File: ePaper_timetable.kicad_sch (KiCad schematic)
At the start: 70 parts, among them J1 USB_C_Receptacle_USB2.0, J2 Conn_01x01_Pin, J3 52435-2471, J4 Conn_01x03_Socket, J5 Charging input - 5V, J6 Conn_01x03_Socket, J7 Conn_01x03_Socket, J8 Conn_01x04_Socket, J9 Battery connector, Q1 BSS138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

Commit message: layout proposition
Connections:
- net Interconnect: now reaches Q3.1, Q3.8
- net USB_DM renamed USB-
- net USB_DP renamed USB+
- no-connect marks 20 -> 19
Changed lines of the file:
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@@
   (no_connect (at 35.56 86.36))
   (no_connect (at 76.2 66.04))
-  (no_connect (at 219.71 131.445))
   (no_connect (at 76.2 45.72))
   (no_connect (at 63.5 247.65))
@@
     (effects (font (size 1.27 1.27)) (justify right bottom))
   )
-  (label "USB_DP" (at 55.88 24.765 90) (fields_autoplaced)
+  (label "USB+" (at 55.88 24.765 90) (fields_autoplaced)
     (effects (font (size 1.27 1.27)) (justify left bottom))
   )
@@
     (effects (font (size 1.27 1.27)) (justify left bottom))
   )
-  (label "USB_DP" (at 104.14 237.49 0) (fields_autoplaced)
+  (label "USB+" (at 104.14 237.49 0) (fields_autoplaced)
     (effects (font (size 1.27 1.27)) (justify left bottom))
   )
@@
     (effects (font (size 1.27 1.27)) (justify left bottom))
   )
+  (label "Interconnect" (at 219.71 131.445 0) (fields_autoplaced)
+    (effects (font (size 1.27 1.27)) (justify left bottom))
+  )
   (label "BOOTSEL" (at 63.5 24.765 90) (fields_autoplaced)
     (effects (font (size 1.27 1.27)) (justify left bottom))
@@
     (effects (font (size 1.27 1.27)) (justify right bottom))
   )
-  (label "USB_DM" (at 104.14 232.41 0) (fields_autoplaced)
-    (effects (font (size 1.27 1.27)) (justify left bottom))
-  )
-  (label "USB_DM" (at 53.34 24.765 90) (fields_autoplaced)
-    (effects (font (size 1.27 1.27)) (justify left bottom))
-  )
+  (label "USB-" (at 104.14 232.41 0) (fields_autoplaced)
+    (effects (font (size 1.27 1.27)) (justify left bottom))
+  )
+  (label "USB-" (at 53.34 24.765 90) (fields_autoplaced)
+    (effects (font (size 1.27 1.27)) (justify left bottom))
+  )

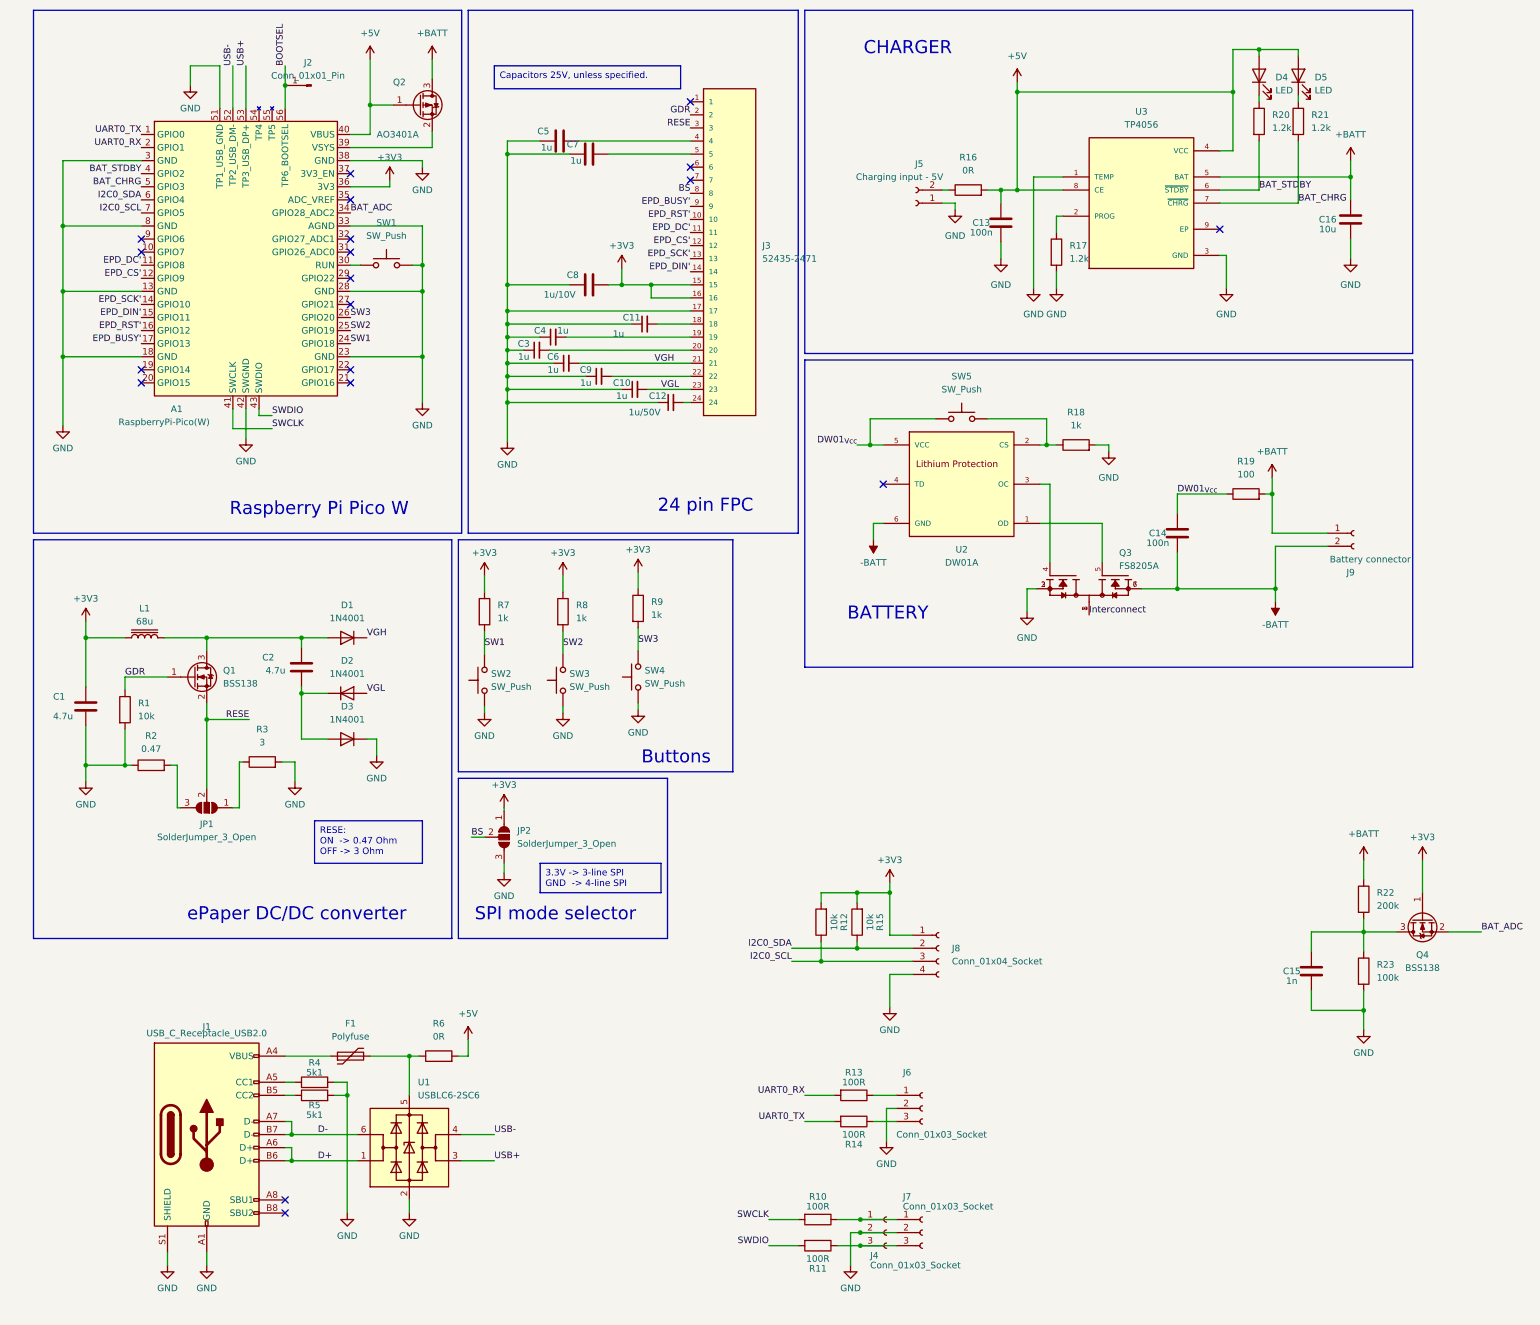
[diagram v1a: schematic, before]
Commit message: Update ePaper_timetable.kicad_sch
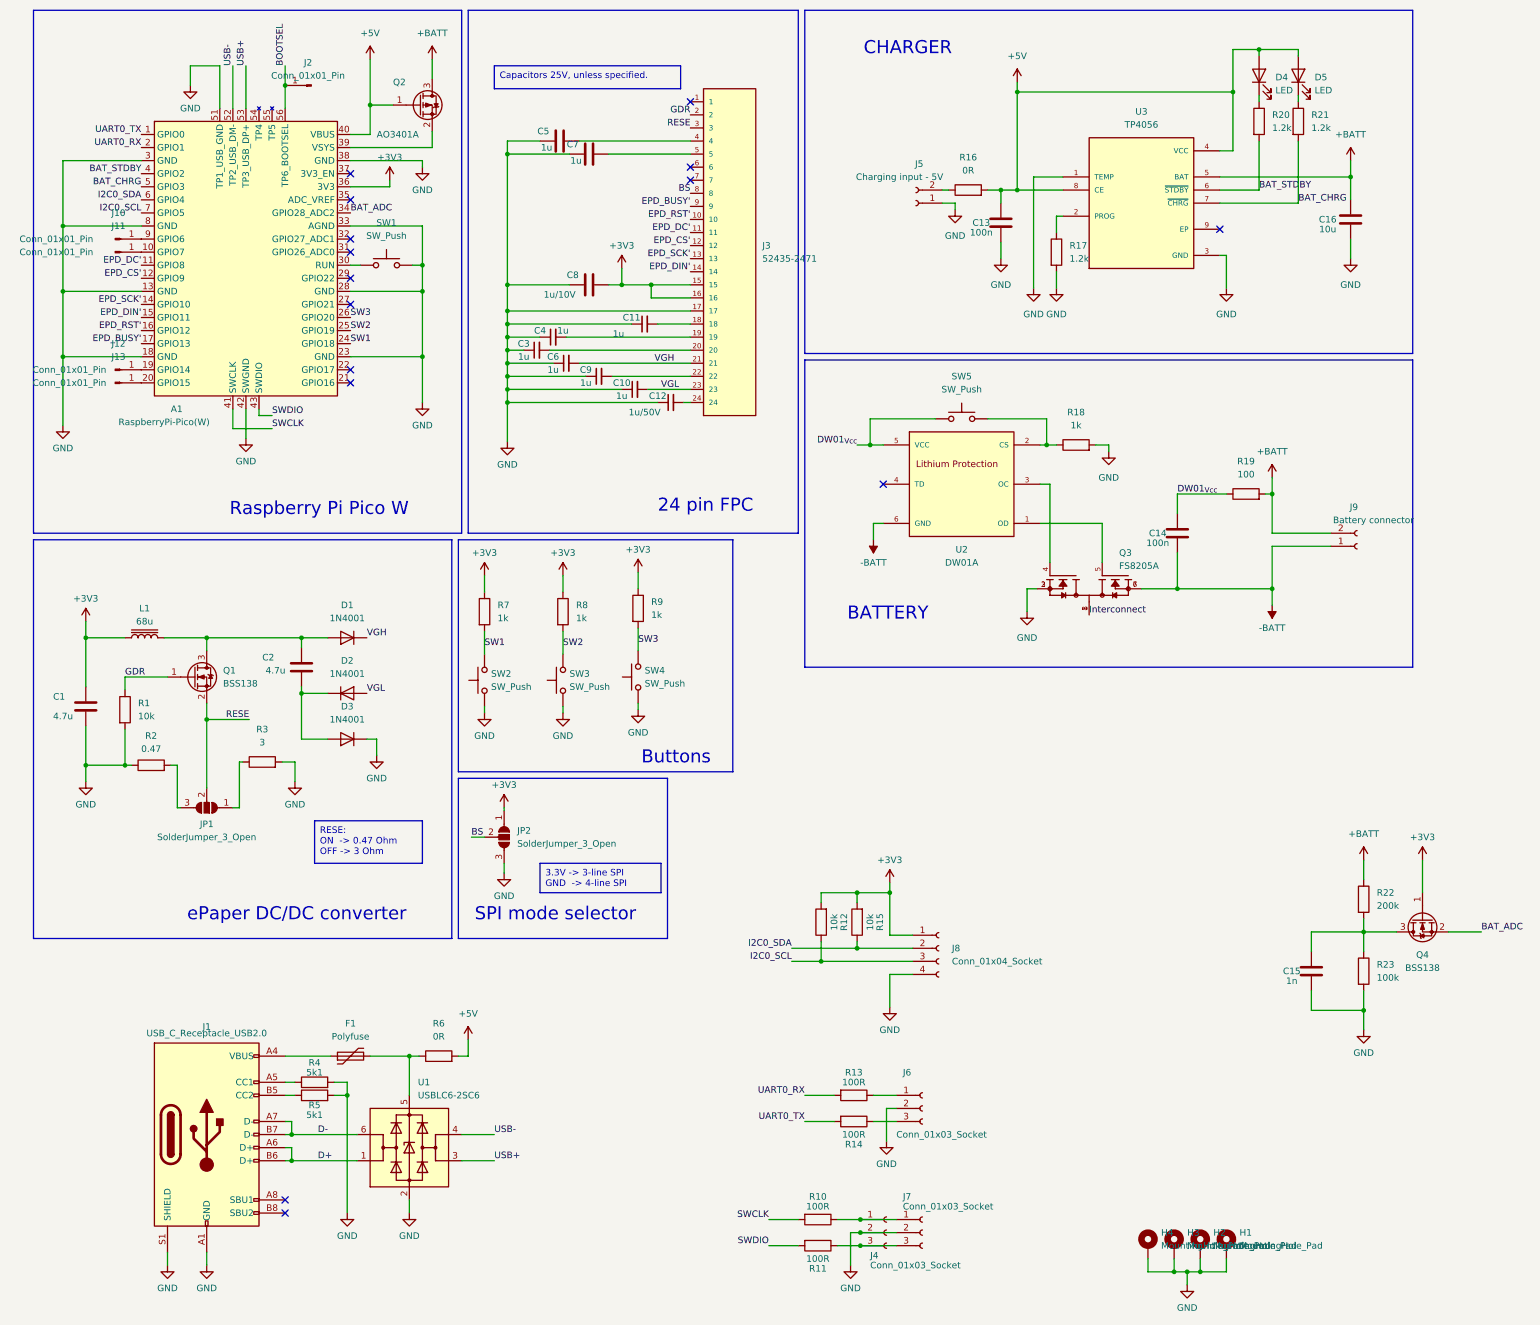
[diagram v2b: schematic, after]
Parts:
- added H1, H2, H3, H4: MountingHole_Pad, MountingHole:MountingHole_3.2mm_M3_Pad, symbol Mechanical:MountingHole_Pad
- added J10, J11, J12, J13: Conn_01x01_Pin, Connector_Wire:SolderWirePad_1x01_SMD_1x2mm, symbol Connector:Conn_01x01_Pin
- J7: footprint Connector_PinSocket_2.54mm:PinSocket_1x03_P2.54mm_Vertical -> Connector_JST:JST_SH_BM03B-SRSS-TB_1x03-1MP_P1.00mm_Vertical
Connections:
- net +BATT: now also J9.2 (Pin_2); no longer J9.1 (Pin_1)
- net -BATT: now also J9.1 (Pin_1); no longer J9.2 (Pin_2)
- net GND: now also H1.1, H2.1, H3.1, H4.1
- net at A1.10 (GPIO7): now also J11.1 (Pin_1)
- net at A1.19 (GPIO14): now also J12.1 (Pin_1)
- net at A1.20 (GPIO15): now also J13.1 (Pin_1)
- net at A1.9 (GPIO6): now also J10.1 (Pin_1)
- no-connect marks 19 -> 15
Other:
- moved on the sheet: J9

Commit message: cosmetic
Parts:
- R19: value 100 -> 100R
- R2: value 0.47 -> 0.47R
- R3: value 3 -> 3R
- R4, R5: value 5k1 -> 5.1k
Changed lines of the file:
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@@
       (effects (font (size 1.27 1.27)))
     )
-    (property "Value" "5k1" (at 69.215 220.345 90)
+    (property "Value" "5.1k" (at 69.215 220.345 90)
       (effects (font (size 1.27 1.27)))
     )
@@
       (effects (font (size 1.27 1.27)))
     )
-    (property "Value" "0.47" (at 37.465 157.48 90)
+    (property "Value" "0.47R" (at 37.465 157.48 90)
       (effects (font (size 1.27 1.27)))
     )
@@
       (effects (font (size 1.27 1.27)))
     )
-    (property "Value" "100" (at 250.19 104.14 90)
+    (property "Value" "100R" (at 250.19 104.14 90)
       (effects (font (size 1.27 1.27)))
     )
@@
       (effects (font (size 1.27 1.27)))
     )
-    (property "Value" "3" (at 59.055 156.21 90)
+    (property "Value" "3R" (at 59.055 156.21 90)
       (effects (font (size 1.27 1.27)))
     )
@@
       (effects (font (size 1.27 1.27)))
     )
-    (property "Value" "5k1" (at 69.215 228.6 90)
-      (effects (font (size 1.27 1.27)))
-    )
+    (property "Value" "5.1k" (at 69.215 228.6 90)
+      (effects (font (size 1.27 1.27)))
+    )
